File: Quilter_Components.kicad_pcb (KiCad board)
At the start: 4 copper layers, 40.4 x 100 mm, 146 parts, among them J1 Conn_01x10_Male, J2 Conn_01x10_Male, J3 Conn_01x10_Male, J4 Eurorack_10_pin_power, U1 TL072, U10 SSI2144, U2 TL074, U3 TL074, U4 TL074, U5 SSI2144, U7 SSI2144, U9 SSI2144

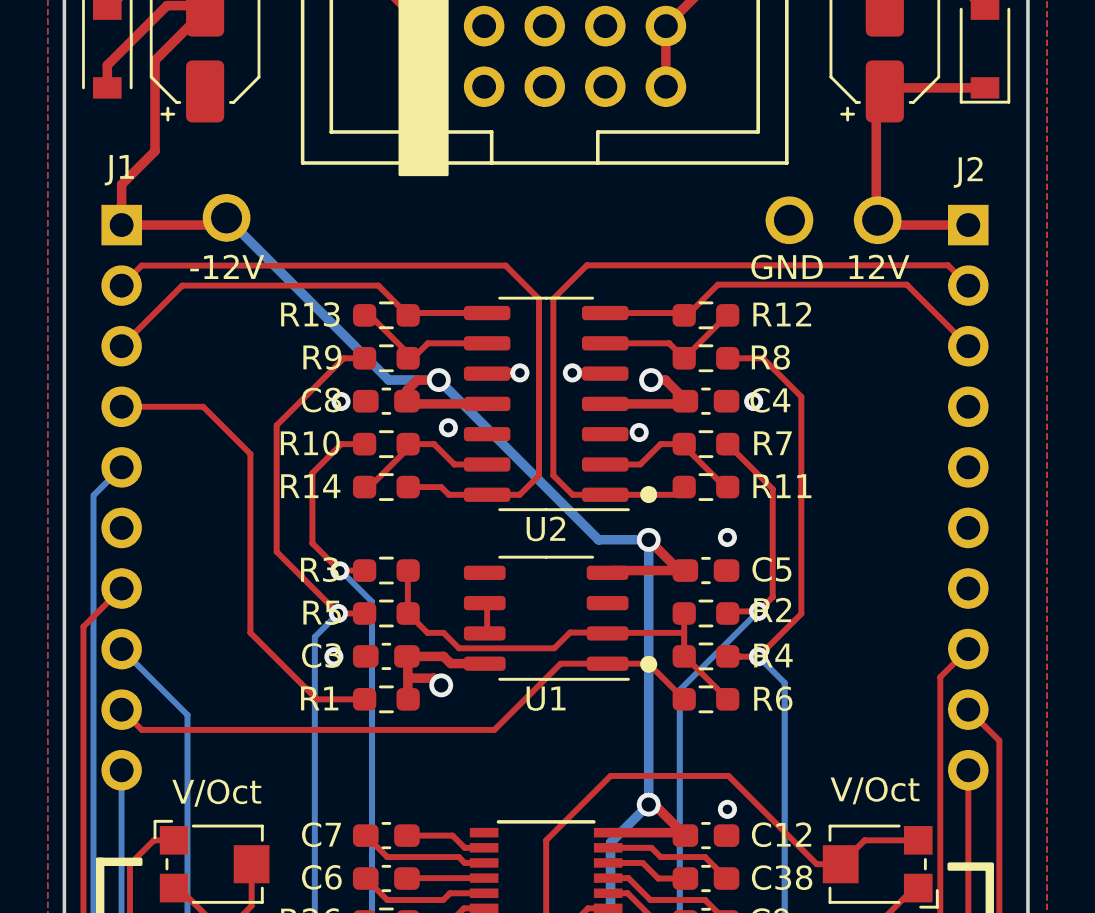
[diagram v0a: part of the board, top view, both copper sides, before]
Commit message: Added op-amp output protection resistors
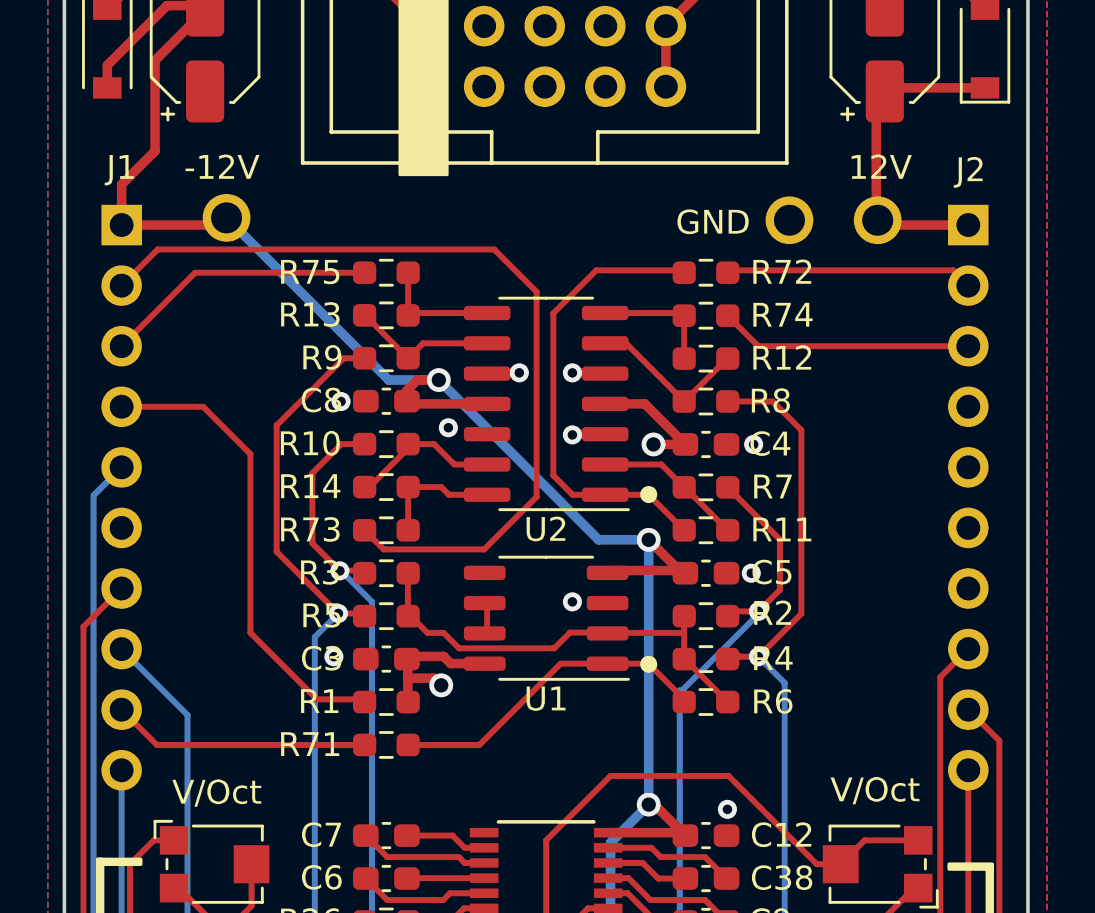
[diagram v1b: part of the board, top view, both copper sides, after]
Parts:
- added R71: 1k, Resistor_SMD:R_0603_1608Metric_Pad0.98x0.95mm_HandSolder, F.Cu at (63.5, 84.6)
- added R72: 1k, Resistor_SMD:R_0603_1608Metric_Pad0.98x0.95mm_HandSolder, F.Cu at (76.9, 64.8)
- added R73: 1k, Resistor_SMD:R_0603_1608Metric_Pad0.98x0.95mm_HandSolder, F.Cu at (63.5, 75.6)
- added R74: 1k, Resistor_SMD:R_0603_1608Metric_Pad0.98x0.95mm_HandSolder, F.Cu at (76.9, 66.6)
- added R75: 1k, Resistor_SMD:R_0603_1608Metric_Pad0.98x0.95mm_HandSolder, F.Cu at (63.5, 64.8)
- moved C4 1.81 mm to (76.9, 72.0)
- moved R11 1.81 mm to (76.9, 75.6)
- moved R12 1.81 mm to (76.9, 68.4)
- moved R7 1.81 mm to (76.9, 73.8)
- moved R8 1.81 mm to (76.9, 70.2)
- moved C5 0.11 mm to (76.9, 77.4)
- moved R3 0.11 mm to (63.5, 77.4)
- moved C3 0.11 mm to (63.5, 81.0)
- moved R1 0.11 mm to (63.5, 82.8)
- moved R2 0.11 mm to (76.9, 79.2)
- moved R4 0.11 mm to (76.9, 81.0)
- moved R5 0.11 mm to (63.5, 79.2)
- moved R6 0.11 mm to (76.9, 82.8)
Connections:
- R11 pad 1: /AUDIO_BUFF1 -> Net-(R11-Pad1)
- R12 pad 1: /AUDIO_BUFF3 -> Net-(R12-Pad1)
- R13 pad 1: /AUDIO_BUFF4 -> Net-(R13-Pad1)
- R14 pad 1: /AUDIO_BUFF2 -> Net-(R14-Pad1)
- R6 pad 1: /AUDIO_MIX -> Net-(R6-Pad1)
- U1 pad 1: /AUDIO_MIX -> Net-(R6-Pad1)
- U2 pad 1: /AUDIO_BUFF1 -> Net-(R11-Pad1)
- U2 pad 14: /AUDIO_BUFF2 -> Net-(R14-Pad1)
- U2 pad 7: /AUDIO_BUFF3 -> Net-(R12-Pad1)
- U2 pad 8: /AUDIO_BUFF4 -> Net-(R13-Pad1)
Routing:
- net /AUDIO_BUFF1: track 31.6 -> 10.4 mm
- net Net-(R11-Pad1): track 0.00 -> 19.5 mm
- net /AUDIO_MIX: track 25.6 -> 10.8 mm
- net Net-(R6-Pad1): track 0.00 -> 13.5 mm
- net /AUDIO_BUFF3: track 16.8 -> 10.6 mm
- net /AUDIO_BUFF4: track 16.8 -> 11.5 mm
- net Net-(R14-Pad1): track 0.00 -> 5.16 mm
- net Net-(R12-Pad1): track 0.00 -> 5.16 mm
- net Net-(R13-Pad1): track 0.00 -> 5.14 mm
- net /AUDIO_BUFF2: track 31.7 -> 35.8 mm
- net /Audio_Out3: track 70.0 -> 68.4 mm
- net /Audio_Out1: track 34.2 -> 32.6 mm
- net +12V: track 240.5 -> 239.2 mm
- net GND: track 4.23 -> 5.60 mm, vias 43 -> 44
- net Net-(R12-Pad2): track 6.04 -> 6.92 mm

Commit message: Generated Gerbers for Production
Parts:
- added kibuzzard-640237A8: G***, kibuzzard-640237A8, F.Cu at (84.1, 60.8)
- added kibuzzard-640237DF: G***, kibuzzard-640237DF, F.Cu at (80.4, 60.8)
- added kibuzzard-640237DF: G***, kibuzzard-640237DF, F.Cu at (88.5, 146.2)
- added kibuzzard-640237FD: G***, kibuzzard-640237FD, F.Cu at (56.9, 60.7)
- moved R6 1.80 mm to (76.9, 84.6)
- moved R4 1.60 mm to (76.9, 82.6)
- moved R2 1.44 mm to (76.9, 80.6)
- moved U1 1.31 mm to (70.2, 80.6)
- moved C5 1.30 mm to (76.9, 78.7)
- moved R11 1.20 mm to (76.9, 76.8)
- moved R7 1.00 mm to (76.9, 74.8)
- moved U2 0.90 mm to (70.2, 71.2)
- moved C4 0.80 mm to (76.9, 72.8)
- moved R8 0.60 mm to (76.9, 70.8)
- moved R12 0.40 mm to (76.9, 68.8)
- moved R74 0.20 mm to (76.9, 66.8)
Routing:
- net Net-(R2-Pad1): track 18.6 -> 21.3 mm
- net /FREQ_POT_5V: track 19.7 -> 17.1 mm
- net /Audio_Out2: track 42.8 -> 45.4 mm
- net /Audio_Out1: track 32.6 -> 34.2 mm
- net /Q_POT: track 125.3 -> 126.8 mm
- net -12V: track 221.1 -> 219.9 mm
- net Net-(R11-Pad1): track 19.5 -> 20.6 mm
- net /AUDIO_BUFF2: track 35.8 -> 36.8 mm
- net /Audio_Out3: track 68.4 -> 69.3 mm
- net /Audio_Out4: track 79.4 -> 78.7 mm
- net GND: track 5.60 -> 5.65 mm, vias 44 -> 47
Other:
- board text removed: "-12V"
- board text removed: "12V"
- board text removed: "GND"

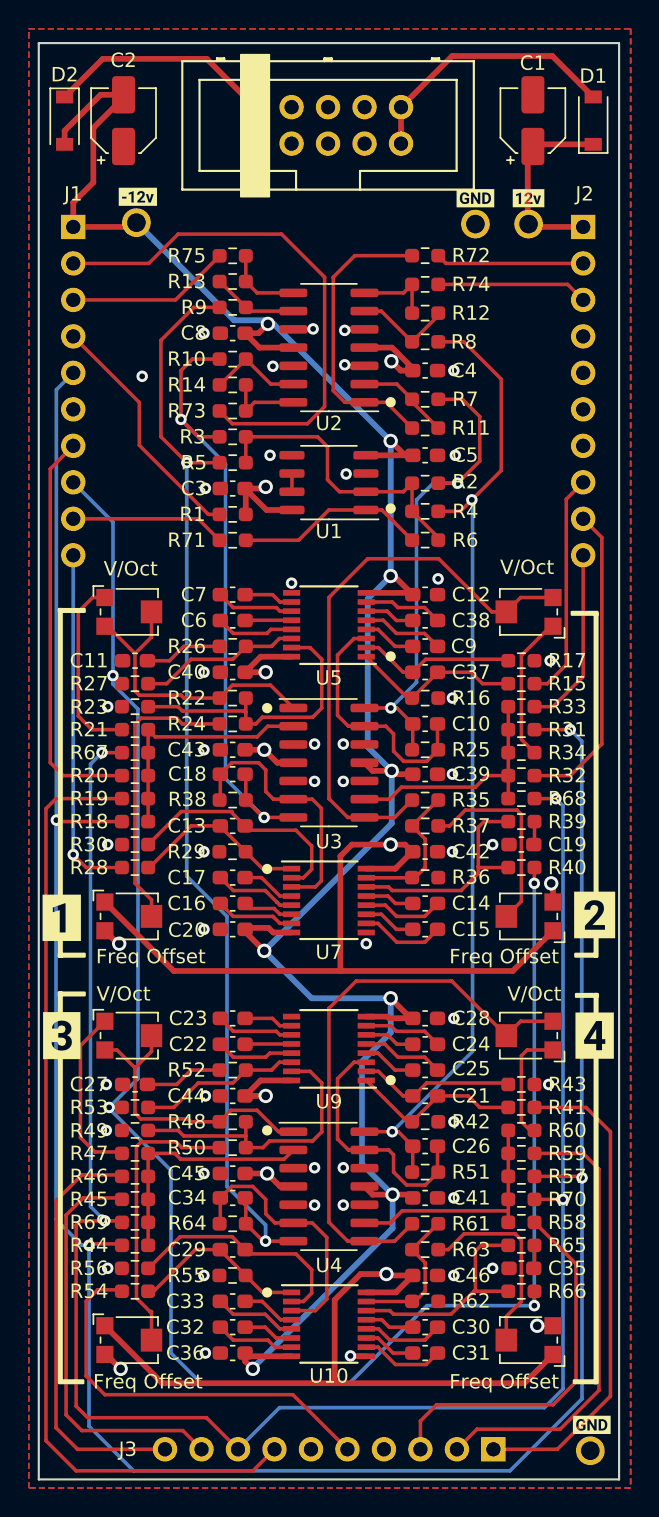
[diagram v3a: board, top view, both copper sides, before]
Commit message: Started adding DC blocking caps to audio outputs
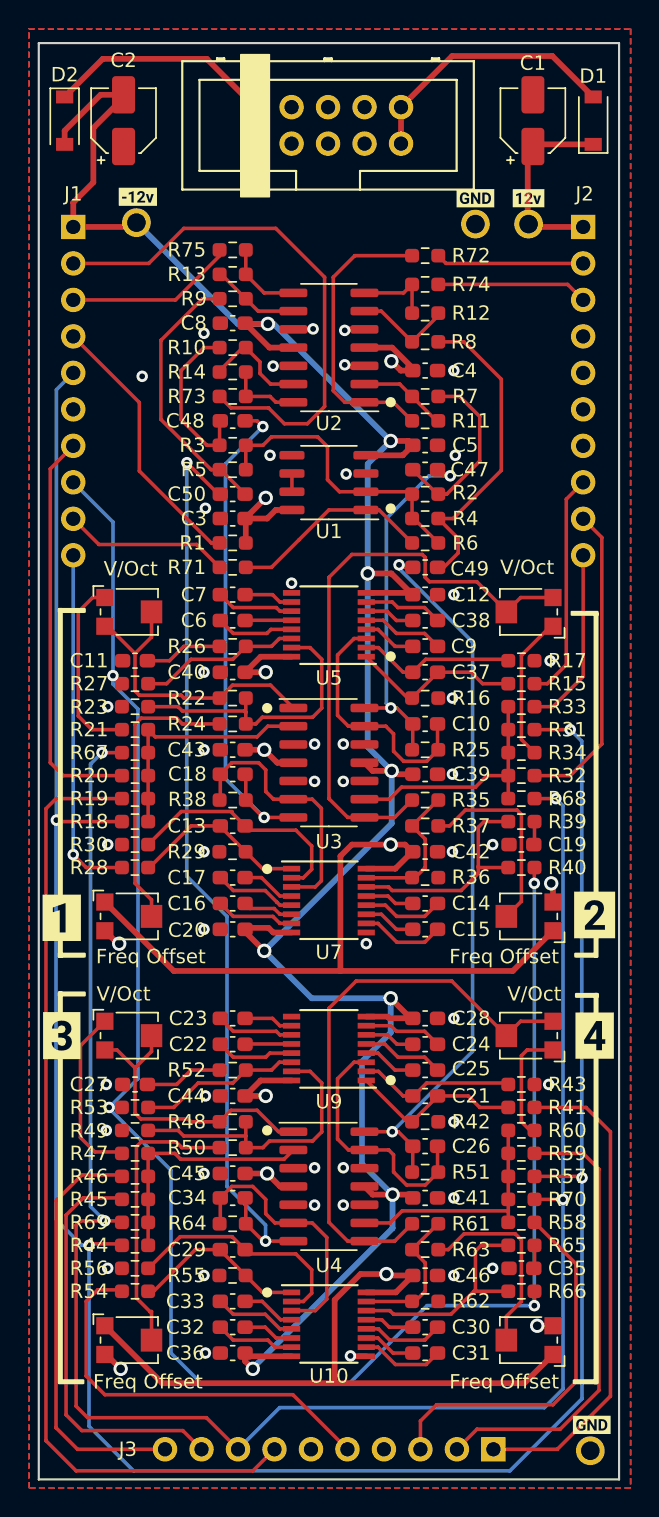
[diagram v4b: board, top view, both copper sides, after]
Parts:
- added C47: 10uF, Capacitor_SMD:C_0603_1608Metric_Pad1.08x0.95mm_HandSolder, F.Cu at (76.9, 79.7)
- added C48: 10uF, Capacitor_SMD:C_0603_1608Metric_Pad1.08x0.95mm_HandSolder, F.Cu at (63.5, 76.3)
- added C49: 10uF, Capacitor_SMD:C_0603_1608Metric_Pad1.08x0.95mm_HandSolder, F.Cu at (76.9, 86.5)
- added C50: 10uF, Capacitor_SMD:C_0603_1608Metric_Pad1.08x0.95mm_HandSolder, F.Cu at (63.5, 81.4)
- moved C3 2.09 mm to (63.5, 83.1)
- moved R1 1.99 mm to (63.5, 84.8)
- moved R71 1.89 mm to (63.5, 86.5)
- moved R73 1.01 mm to (63.5, 74.6)
- moved R14 0.90 mm to (63.5, 72.9)
- moved R10 0.80 mm to (63.5, 71.2)
- moved R2 0.76 mm to (76.9, 81.4)
- moved C5 0.70 mm to (76.9, 78.0)
- moved C8 0.70 mm to (63.5, 69.5)
- moved R9 0.60 mm to (63.5, 67.8)
- moved R3 0.59 mm to (63.5, 78.0)
- moved R11 0.50 mm to (76.9, 76.3)
- moved R13 0.50 mm to (63.5, 66.1)
- moved R4 0.50 mm to (76.9, 83.1)
- moved R5 0.49 mm to (63.5, 79.7)
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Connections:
- C10 pad 1: /Audio_Out1 -> Net-(C10-Pad1)
- C18 pad 1: /Audio_Out2 -> Net-(C18-Pad1)
- C26 pad 1: /Audio_Out3 -> Net-(C26-Pad1)
- C34 pad 1: /Audio_Out4 -> Net-(C34-Pad1)
- R25 pad 1: /Audio_Out1 -> Net-(C10-Pad1)
- R38 pad 1: /Audio_Out2 -> Net-(C18-Pad1)
- R51 pad 1: /Audio_Out3 -> Net-(C26-Pad1)
- R64 pad 1: /Audio_Out4 -> Net-(C34-Pad1)
- U3 pad 14: /Audio_Out1 -> Net-(C10-Pad1)
- U3 pad 7: /Audio_Out2 -> Net-(C18-Pad1)
- U4 pad 14: /Audio_Out3 -> Net-(C26-Pad1)
- U4 pad 7: /Audio_Out4 -> Net-(C34-Pad1)
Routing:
- net Net-(C34-Pad1): track 0.00 -> 65.3 mm, vias 0 -> 2
- net /Audio_Out4: track 78.7 -> 18.8 mm, vias 2 -> 0
- net Net-(C26-Pad1): track 0.00 -> 50.5 mm, vias 0 -> 2
- net /Audio_Out3: track 69.3 -> 22.4 mm, vias 2 -> 0
- net Net-(C18-Pad1): track 0.00 -> 36.4 mm, vias 0 -> 2
- net /Audio_Out2: track 45.4 -> 11.9 mm, vias 2 -> 0
- net Net-(C10-Pad1): track 0.00 -> 25.7 mm, vias 0 -> 2
- net /Audio_Out1: track 34.2 -> 12.9 mm, vias 2 -> 0
- net Net-(R35-Pad2): track 39.5 -> 41.4 mm
- net /FREQ_POT_5V: track 17.1 -> 18.9 mm
- net -12V: track 219.9 -> 221.6 mm
- net Net-(R6-Pad1): track 13.3 -> 14.2 mm
- net Net-(R10-Pad1): track 6.60 -> 7.42 mm
- net /AUDIO_MIX: track 10.8 -> 11.6 mm
- net /AUDIO_BUFF2: track 36.8 -> 37.5 mm
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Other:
- board text added: "Quilter Components v2.0 Mountjoy Modular 2023"
- board text removed: "Quilter Components v1.0 Mountjoy Modular"

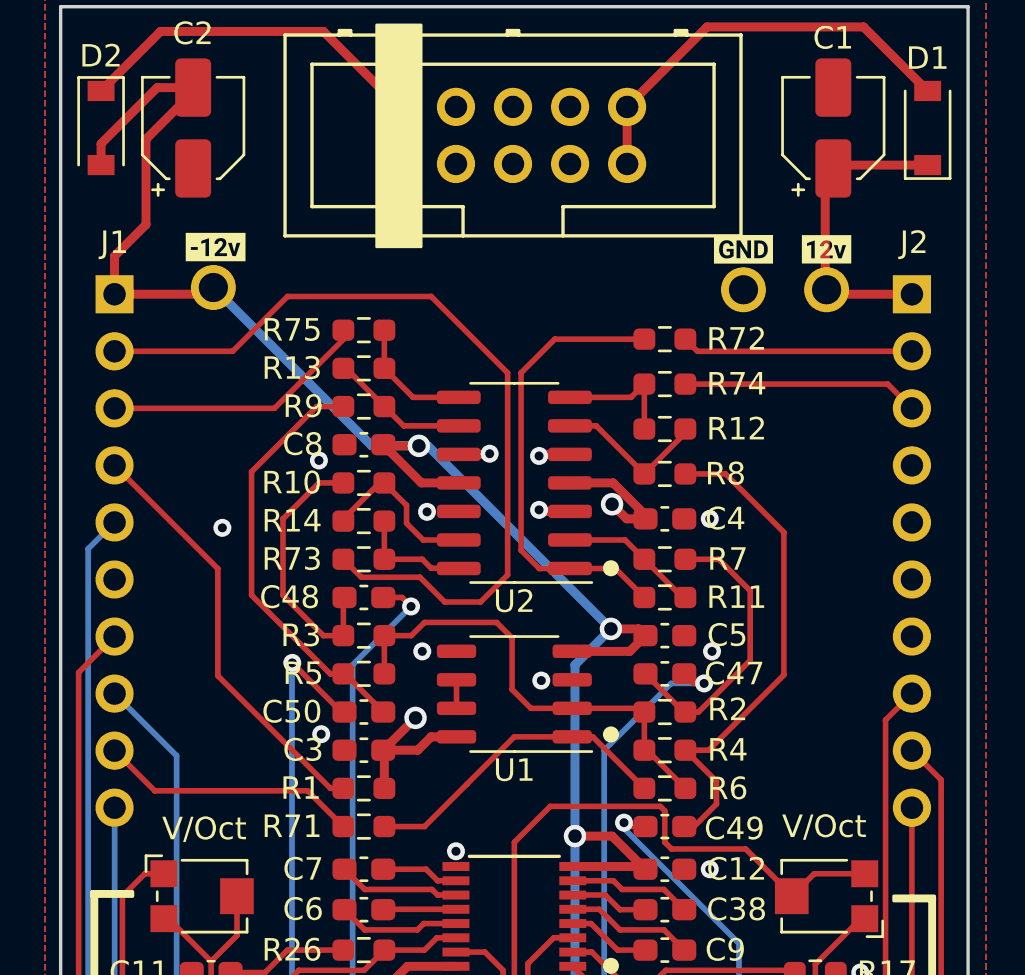
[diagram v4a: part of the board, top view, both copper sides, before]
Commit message: Updates for v2, including dc blocking caps on output
Also adjusted lower range of cutoff knob and tweaked various resistor values
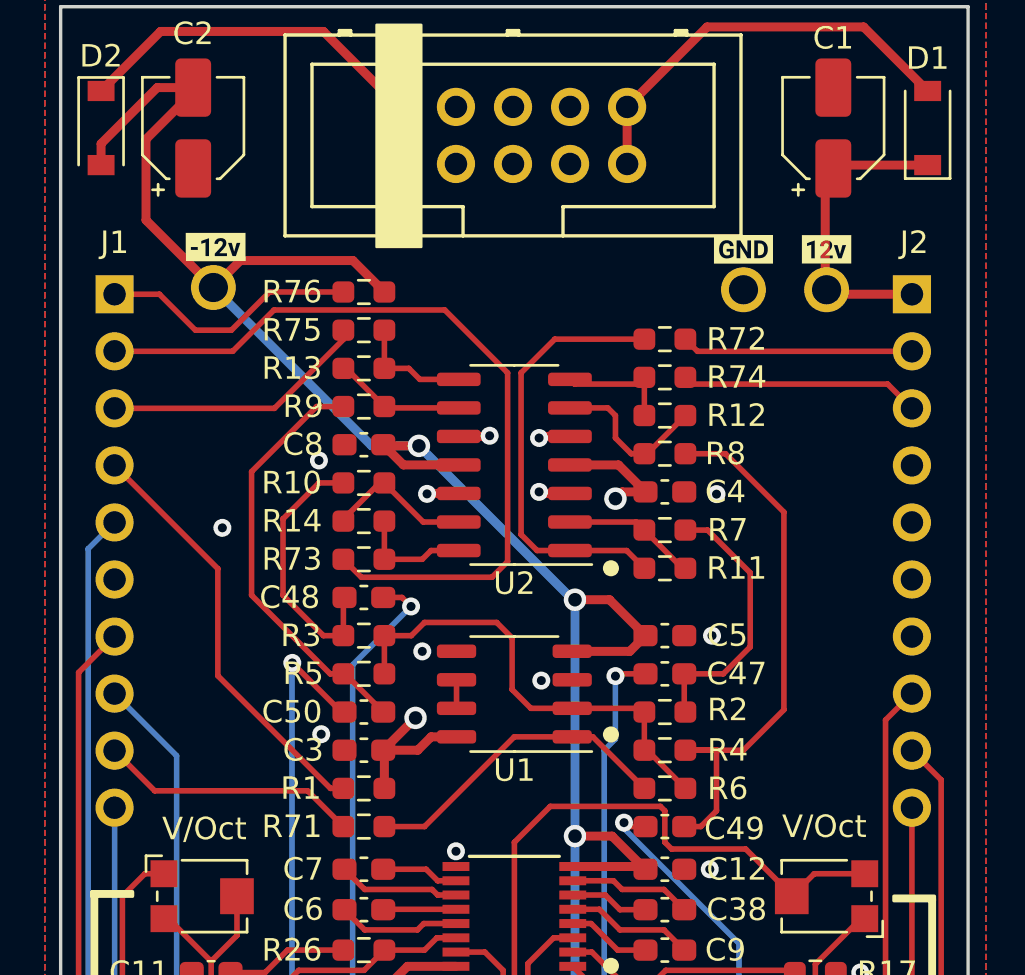
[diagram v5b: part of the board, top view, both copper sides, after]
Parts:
- added R76: 14k, Resistor_SMD:R_0603_1608Metric_Pad0.98x0.95mm_HandSolder, F.Cu at (63.5, 62.7)
- C11, C19, C27, C35: value 10nF -> 10nF_C0G
- C14, C15, C16, C22, C23, C24, C30, C31, C32, C38, C6, C7: value 6.8nF -> 6.8nF_C0G
- C17, C25, C33, C9: value 560pF -> 560pF_C0G
- R27, R40, R53, R66: value 27k -> 24k
- R6: value 10k -> 4.7k
- moved R11 1.30 mm to (76.9, 75.0)
- moved R7 1.30 mm to (76.9, 73.3)
- moved C4 1.20 mm to (76.9, 71.6)
- moved R8 0.90 mm to (76.9, 69.9)
- moved U2 0.80 mm to (70.2, 70.4)
- moved R12 0.60 mm to (76.9, 68.2)
- moved R74 0.30 mm to (76.9, 66.5)
- turned C47 to 180 degrees
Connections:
- J1 pad 1: -12V -> /FREQ_POT_-5V
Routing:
- net /FREQ_POT_-5V: track 0.00 -> 11.6 mm
- net -12V: track 221.6 -> 226.2 mm
- net /Audio_Out3: track 22.4 -> 25.2 mm
- net Net-(C10-Pad1): track 25.7 -> 23.8 mm
- net /AUDIO_BUFF2: track 37.5 -> 35.8 mm
- net GND: track 5.65 -> 7.07 mm
- net Net-(R11-Pad1): track 20.4 -> 19.4 mm
- net Net-(R10-Pad1): track 7.42 -> 6.62 mm
- net /Audio_Out1: track 12.9 -> 12.2 mm
